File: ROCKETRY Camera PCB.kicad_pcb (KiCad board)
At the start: 2 copper layers, 111.8 x 75.7 mm, 38 parts, among them J1 Conn_01x03_Pin, J2 Conn_01x01_Pin, J3 Conn_01x01_Pin, J4 Conn_01x01_Pin, Q1 IRF7780M, U1 3.4v, U2 3.4v, U4 AP62200WU

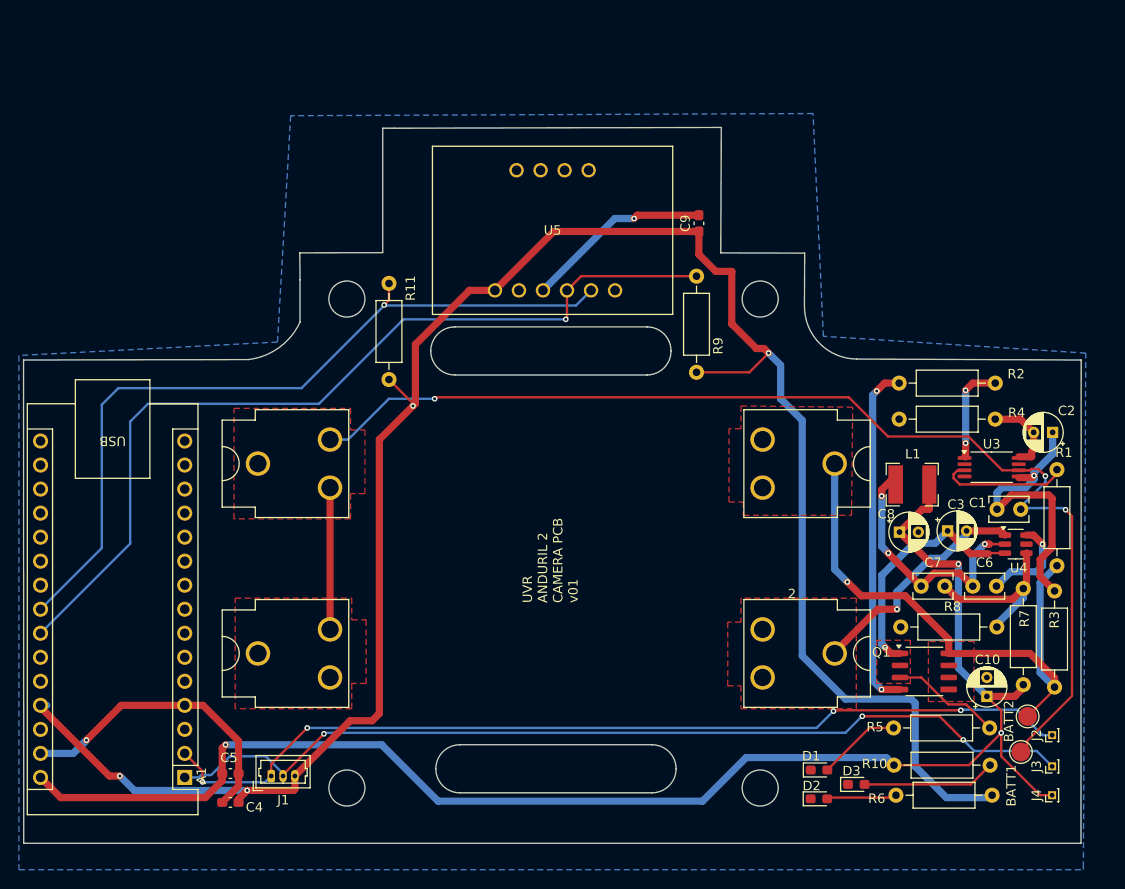
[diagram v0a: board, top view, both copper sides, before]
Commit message: swapped tht components with smt, in progress of routing traces. Board will be waaaaay cleaner
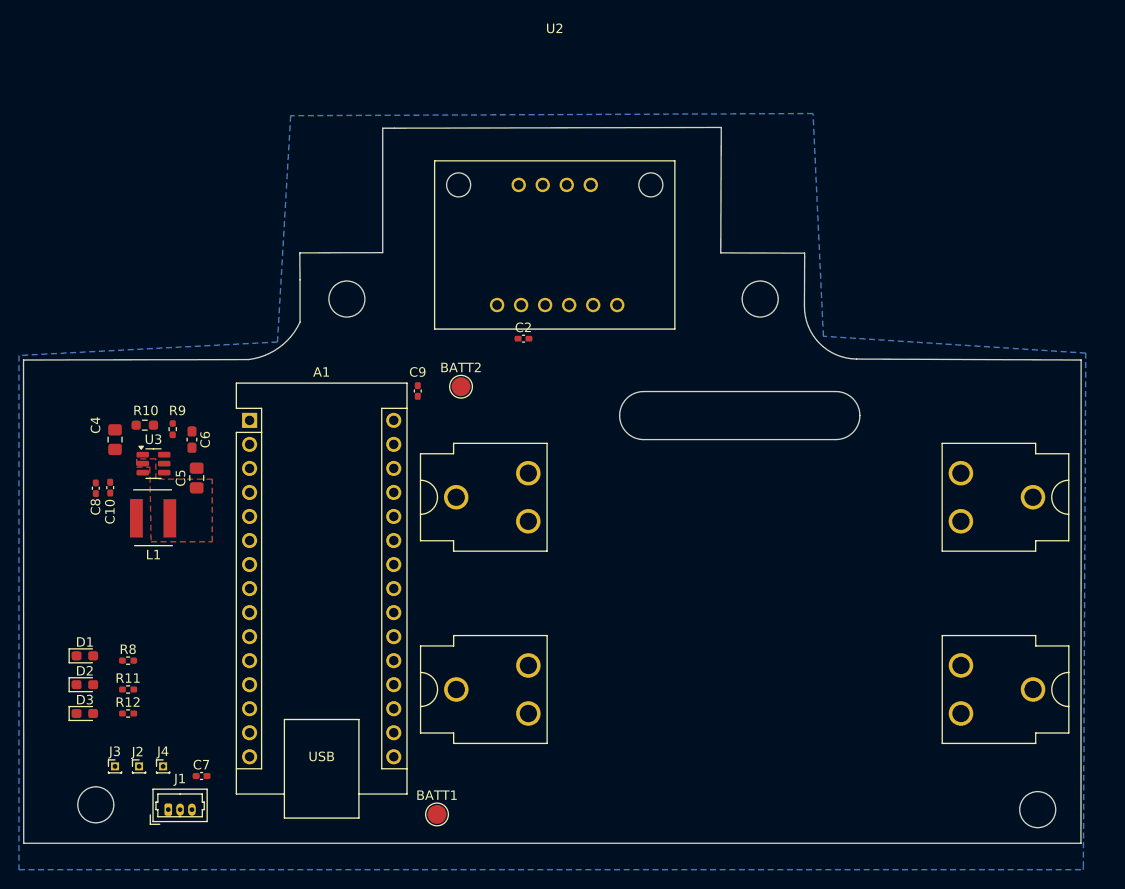
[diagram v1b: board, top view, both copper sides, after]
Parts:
- removed C1: 0.1uF, Capacitor_THT:C_Rect_L4.0mm_W2.5mm_P2.50mm
- removed C3: 10uF, Capacitor_THT:CP_Radial_D4.0mm_P2.00mm
- removed Q1: IRF7780M, Package_SO:SO-8_3.9x4.9mm_P1.27mm
- removed R1, R2: 5.1k, Resistor_THT:R_Axial_DIN0207_L6.3mm_D2.5mm_P10.16mm_Horizontal
- removed R3: 1k, Resistor_THT:R_Axial_DIN0207_L6.3mm_D2.5mm_P10.16mm_Horizontal
- removed R4: 51, Resistor_THT:R_Axial_DIN0207_L6.3mm_D2.5mm_P10.16mm_Horizontal
- removed R5, R6: 10k, Resistor_THT:R_Axial_DIN0207_L6.3mm_D2.5mm_P10.16mm_Horizontal
- removed R7: 52k, Resistor_THT:R_Axial_DIN0207_L6.3mm_D2.5mm_P10.16mm_Horizontal
- removed U1: 3.4v, CUSTOM_footprints:BatteryClip_Keystone_54_D16-19mm
- removed U4: AP62200WU, Package_TO_SOT_SMD:TSOT-23-6
- removed U5: ~, CUSTOM_footprints:ADX375L
- added BT1: 3.6V, CUSTOM_footprints:BatteryClip_Keystone_54_D16-19mm, F.Cu at (127.5, 89.4)
- added BT2: 3.6V, CUSTOM_footprints:BatteryClip_Keystone_54_D16-19mm, F.Cu at (127.5, 109.7)
- added R12: 1k, Resistor_SMD:R_0402_1005Metric_Pad0.72x0.64mm_HandSolder, F.Cu at (94.9, 112.3)
- C10, C8: footprint Capacitor_THT:CP_Radial_D4.0mm_P2.00mm -> Capacitor_SMD:C_0402_1005Metric_Pad0.74x0.62mm_HandSolder
- C2: value 2.2uF -> 100nF; footprint Capacitor_THT:CP_Radial_D4.0mm_P2.00mm -> Capacitor_SMD:C_0402_1005Metric_Pad0.74x0.62mm_HandSolder
- C4: value 100uF -> 10uF; footprint Capacitor_SMD:C_0603_1608Metric_Pad1.08x0.95mm_HandSolder -> Capacitor_SMD:C_0805_2012Metric_Pad1.18x1.45mm_HandSolder
- C5: value 100nF -> 330nF; footprint Capacitor_SMD:C_0603_1608Metric_Pad1.08x0.95mm_HandSolder -> Capacitor_SMD:C_0805_2012Metric_Pad1.18x1.45mm_HandSolder
- C6: value 200nF -> 100pF; footprint Capacitor_THT:C_Rect_L4.0mm_W2.5mm_P2.50mm -> Capacitor_SMD:C_0603_1608Metric_Pad1.08x0.95mm_HandSolder
- C7: value 20pF -> 100nF; footprint Capacitor_THT:C_Rect_L4.0mm_W2.5mm_P2.50mm -> Capacitor_SMD:C_0402_1005Metric_Pad0.74x0.62mm_HandSolder
- C9: footprint Capacitor_SMD:C_0603_1608Metric_Pad1.08x0.95mm_HandSolder -> Capacitor_SMD:C_0402_1005Metric_Pad0.74x0.62mm_HandSolder
- L1: footprint Inductor_SMD:L_Bourns-SRN5040 -> Inductor_SMD:BOURNS_SRN5040_CUSTOM
- R10: footprint Resistor_THT:R_Axial_DIN0207_L6.3mm_D2.5mm_P10.16mm_Horizontal -> Resistor_SMD:R_0603_1608Metric_Pad0.98x0.95mm_HandSolder
- R11, R8: value 10k -> 1k; footprint Resistor_THT:R_Axial_DIN0207_L6.3mm_D2.5mm_P10.16mm_Horizontal -> Resistor_SMD:R_0402_1005Metric_Pad0.72x0.64mm_HandSolder
- R9: value 10k -> 52.3k; footprint Resistor_THT:R_Axial_DIN0207_L6.3mm_D2.5mm_P10.16mm_Horizontal -> Resistor_SMD:R_0402_1005Metric_Pad0.72x0.64mm_HandSolder
- U2: value 3.4v -> ~; footprint CUSTOM_footprints:BatteryClip_Keystone_54_D16-19mm -> CUSTOM_footprints:ADX375L
- U3: value ~ -> AP62200WU; footprint Package_SO:TSSOP-8_4.4x3mm_P0.65mm -> Package_TO_SOT_SMD:TSOT-23-6
- moved J3 99.1 mm to (93.5, 117.9), turned to 0 degrees
- moved J2 96.6 mm to (96.0, 117.9), turned to 0 degrees
- moved C10 95.3 mm to (93.0, 88.4)
- moved J4 94.0 mm to (98.6, 117.9), turned to 0 degrees
- moved R8 91.9 mm to (94.9, 106.7), turned to 0 degrees
- moved U3 88.6 mm to (97.5, 85.9)
- moved R10 87.0 mm to (96.6, 81.8), turned to 180 degrees
- moved C8 85.1 mm to (91.4, 88.5), turned to 90 degrees
- moved C6 84.0 mm to (101.6, 83.3), turned to -90 degrees
- moved D3 81.9 mm to (90.3, 112.3)
- moved L1 80.9 mm to (97.5, 90.4)
- moved C7 78.7 mm to (102.6, 118.9)
- moved D1 78.5 mm to (90.3, 106.2)
- moved D2 78.5 mm to (90.3, 109.2)
- moved BATT2 69.3 mm to (130.0, 77.7)
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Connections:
- A1 pad 23: /A4 -> /SDA
- A1 pad 24: /A5 -> /SCL
- A1 pad 27: /+5V -> unconnected-(A1-+5V-Pad27)
- A1 pad 30: /5V -> +5V
- BATT1 pad 1: /V-mid -> +BATT
- BATT2 pad 1: /V-BATT+ -> VCC
- C10 pad 1: /5V -> +5V
- C2 pad 1: Net-(U3-VDD) -> +5V
- C2 pad 2: Net-(U3-VSS) -> GND
- C4 pad 1: /+5V -> VCC
- C4 pad 2: GND -> Net-(BT2--)
- C5 pad 1: GND -> Net-(U3-SW)
- C5 pad 2: /5V -> Net-(U3-BST)
- C6 pad 1: Net-(U4-SW) -> +5V
- C6 pad 2: Net-(U4-BST) -> Net-(U3-FB)
- C7 pad 1: Net-(U4-SW) -> +5V
- C7 pad 2: Net-(U4-FB) -> GND
- C8 pad 1: /5V -> +5V
- C9 pad 1: /+5V -> GND
- C9 pad 2: GND -> +5V
- J1 pad 3: /+5V -> +5V
- J4 pad 1: /5V -> +5V
- L1 pad 1: Net-(U4-SW) -> Net-(U3-SW)
- L1 pad 2: /5V -> +5V
- R10 pad 1: /5V -> Net-(U3-FB)
- R10 pad 2: Net-(D3-A) -> GND
- R11 pad 1: /+5V -> +5V
- R11 pad 2: /A4 -> Net-(D2-A)
- R8 pad 1: Net-(U4-FB) -> VCC
- R8 pad 2: GND -> Net-(D1-A)
- R9 pad 1: /+5V -> +5V
- R9 pad 2: /A5 -> Net-(U3-FB)
- U2 pad 1: /V-mid -> GND
- U2 pad 2: Net-(U2--) -> unconnected-(U2-I2-Pad2)
- U3 pad 1: /DOP -> VCC
- U3 pad 2: unconnected-(U3-COP-Pad2) -> Net-(U3-SW)
- U3 pad 3: /VMP -> Net-(BT2--)
- U3 pad 4: unconnected-(U3-CTL-Pad4) -> Net-(U3-BST)
- U3 pad 5: Net-(U3-VDD) -> unconnected-(U3-EN-Pad5)
- U3 pad 6: /V-mid -> Net-(U3-FB)
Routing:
- net /+5V: track 214.9 -> 0.00 mm, vias 4 -> 0
- net /5V: track 161.4 -> 0.00 mm, vias 3 -> 0
- net /V-mid: track 133.4 -> 0.00 mm, vias 3 -> 0
- net Net-(A1-D0/RX): track 98.9 -> 0.00 mm, vias 4 -> 0
- net Net-(A1-D1/TX): track 98.7 -> 0.00 mm, vias 3 -> 0
- net /A5: track 94.3 -> 0.00 mm, vias 1 -> 0
- net /A4: track 83.7 -> 0.00 mm, vias 1 -> 0
- net /V-BATT+: track 59.5 -> 0.00 mm, vias 1 -> 0
- net GND: track 53.2 -> 0.00 mm, vias 2 -> 0
- net /+7.4V: track 37.3 -> 0.00 mm, vias 1 -> 0
- net Net-(Q1-G): track 36.8 -> 0.00 mm, vias 2 -> 0
- net Net-(U3-VDD): track 31.0 -> 0.00 mm, vias 1 -> 0
- net Net-(U4-SW): track 27.7 -> 0.00 mm, vias 3 -> 0
- net Net-(U2--): track 24.9 -> 0.00 mm, vias 1 -> 0
- net Net-(U4-FB): track 18.9 -> 0.00 mm
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- added copper zone on F.Cu, net Net-(U3-SW)
- removed copper zone on F.Cu, net /+7.4V
- removed copper zone on F.Cu, net /V-BATT+
- removed copper zone on F.Cu, net /V-mid
- removed copper zone on F.Cu, net Net-(U2--)
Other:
- outline, holes or cut-outs redrawn
- board text removed: "2"
- board text removed: "UVR ANDURIL 2 CAMERA PCB v01"

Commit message: pcb ready for final review/ ordering
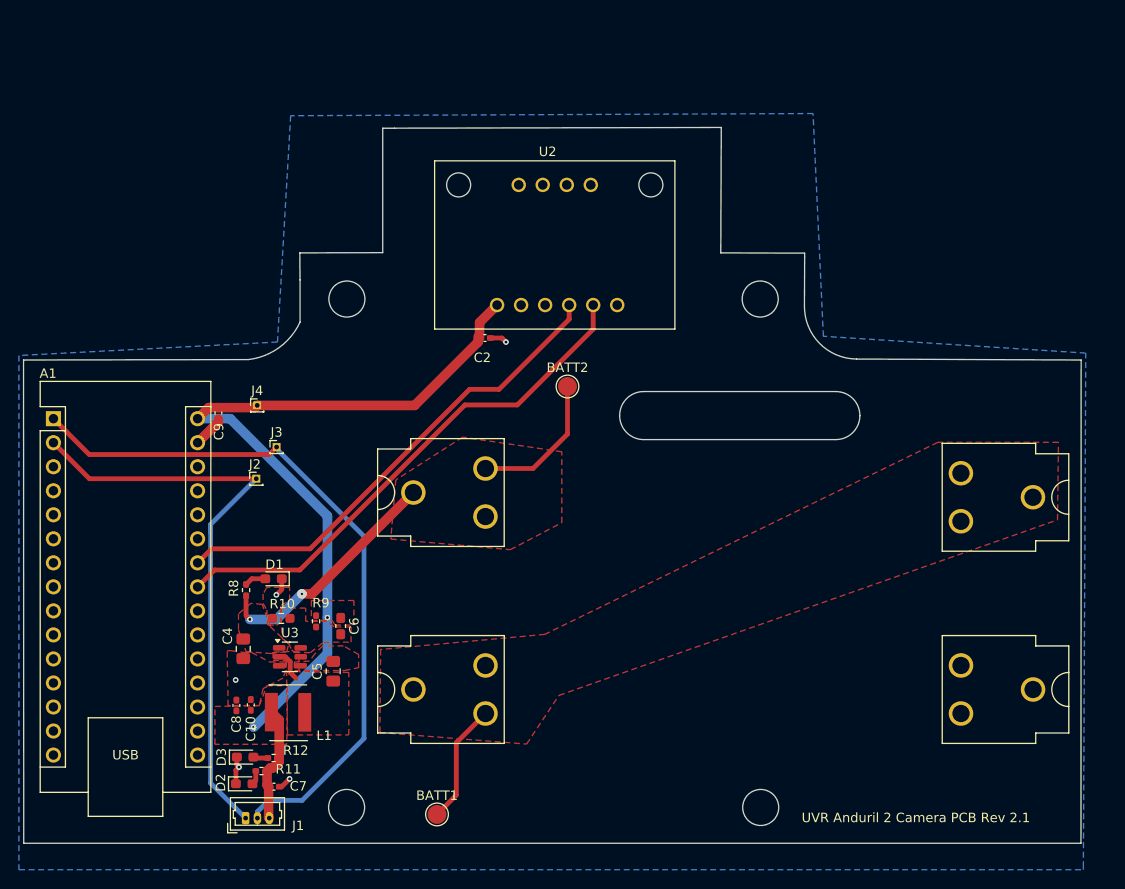
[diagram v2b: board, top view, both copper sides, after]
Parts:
- moved J4 39.4 mm to (108.5, 79.7)
- moved J3 37.8 mm to (110.5, 84.1)
- moved J2 32.8 mm to (108.4, 87.5)
- moved C10 27.4 mm to (107.8, 111.4)
- moved C8 27.4 mm to (106.3, 111.4)
- moved L1 27.0 mm to (111.7, 113.3), turned to 180 degrees
- moved C4 25.9 mm to (107.0, 105.4)
- moved R9 25.3 mm to (114.7, 102.5)
- moved C6 25.2 mm to (117.3, 103.0)
- moved C5 25.0 mm to (116.5, 107.8)
- moved R10 25.0 mm to (111.0, 102.2)
- moved U3 25.0 mm to (112.0, 106.3)
- moved D1 21.5 mm to (110.2, 98.0), turned to 180 degrees
- moved C9 21.2 mm to (104.4, 80.5), turned to 90 degrees
- moved A1 20.7 mm to (87.0, 81.1)
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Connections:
- BT2 pad 2: Net-(BT2--) -> GND
- C4 pad 2: Net-(BT2--) -> GND
- D1 pad 1: Net-(D1-K) -> GND
- D2 pad 1: Net-(D2-K) -> GND
- D3 pad 1: Net-(D3-K) -> GND
- U3 pad 3: Net-(BT2--) -> GND
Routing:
- net +5V: track 0.00 -> 93.7 mm, vias 0 -> 2
- net Net-(A1-D1/TX): track 0.00 -> 75.3 mm
- net Net-(A1-D0/RX): track 0.00 -> 63.0 mm
- net /SDA: track 0.00 -> 55.6 mm
- net /SCL: track 0.00 -> 51.4 mm
- net VCC: track 0.00 -> 40.6 mm, vias 0 -> 2
- net +BATT: track 0.00 -> 12.8 mm
- net GND: track 0.00 -> 11.7 mm, vias 0 -> 5
- net Net-(U3-SW): track 0.00 -> 3.40 mm
- net Net-(D1-A): track 0.00 -> 2.27 mm
- net Net-(D3-A): track 0.00 -> 1.57 mm
- net Net-(D2-A): track 0.00 -> 1.50 mm
- added copper zone on F.Cu, net +5V
- added copper zone on F.Cu, net +BATT
- added copper zone on F.Cu, net GND
- added copper zone on F.Cu, net Net-(U3-BST)
- added copper zone on F.Cu, net Net-(U3-FB)
- added copper zone on F.Cu, net VCC
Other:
- outline, holes or cut-outs redrawn
- rule pad_to_mask_clearance: 0 -> 0.038
- board text added: "UVR Anduril 2 Camera PCB Rev 2.1"

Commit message: adding curves to pcb edges
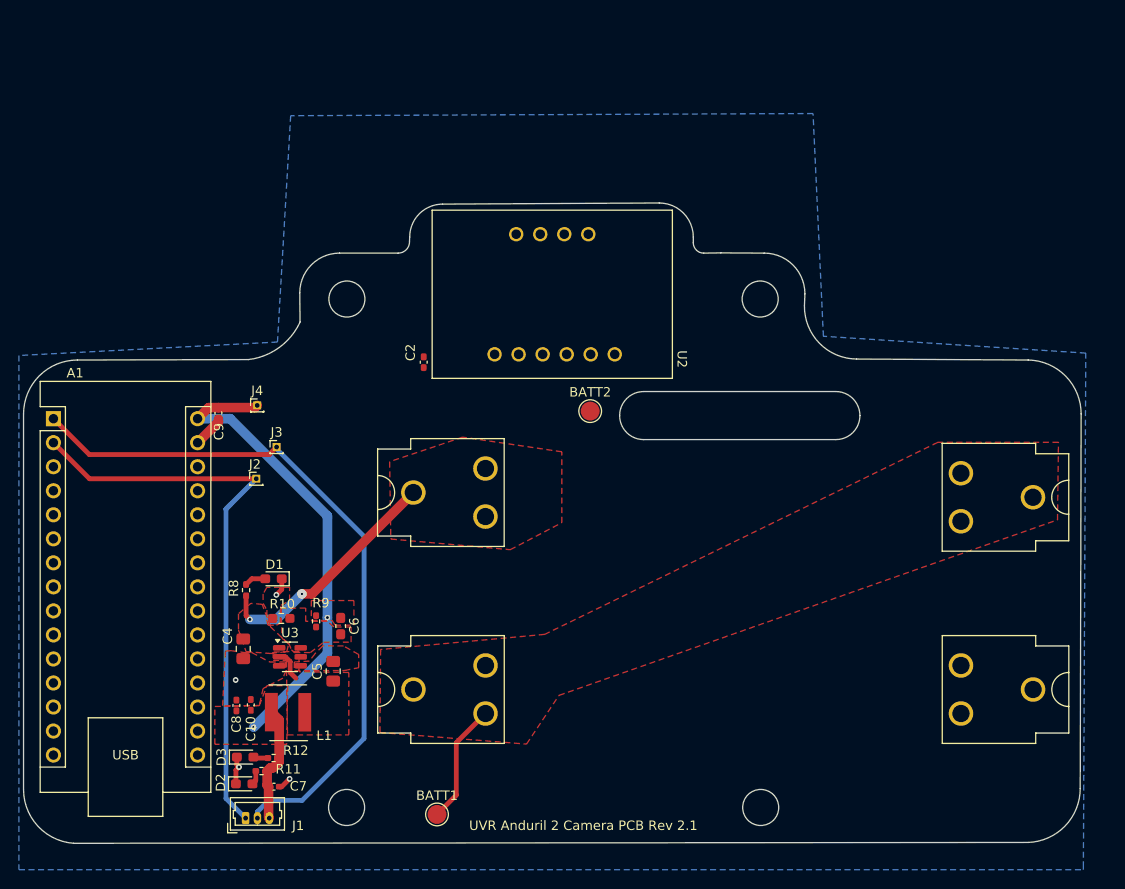
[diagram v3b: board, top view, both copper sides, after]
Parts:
- moved C2 6.96 mm to (126.1, 75.1), turned to 90 degrees
- moved U2 5.22 mm to (139.7, 68.0)
- moved BATT2 3.54 mm to (143.7, 80.3)
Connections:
- C4 pad 1: VCC -> Net-(J5-Pin_1)
- D2 pad 1: GND -> Net-(D2-K)
- R8 pad 1: VCC -> Net-(J5-Pin_1)
- U3 pad 1: VCC -> Net-(J5-Pin_1)
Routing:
- net /SDA: track 55.6 -> 0.00 mm
- net /SCL: track 51.4 -> 0.00 mm
- net +5V: track 93.7 -> 62.8 mm
- net VCC: track 40.6 -> 25.4 mm
- net GND: track 11.7 -> 9.89 mm, vias 5 -> 4
- net Net-(A1-D0/RX): track 63.0 -> 61.8 mm
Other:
- board size 111.8 x 75.7 mm -> 111.8 x 67.7 mm

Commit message: added curves to pcb edges, added connector for screw switch
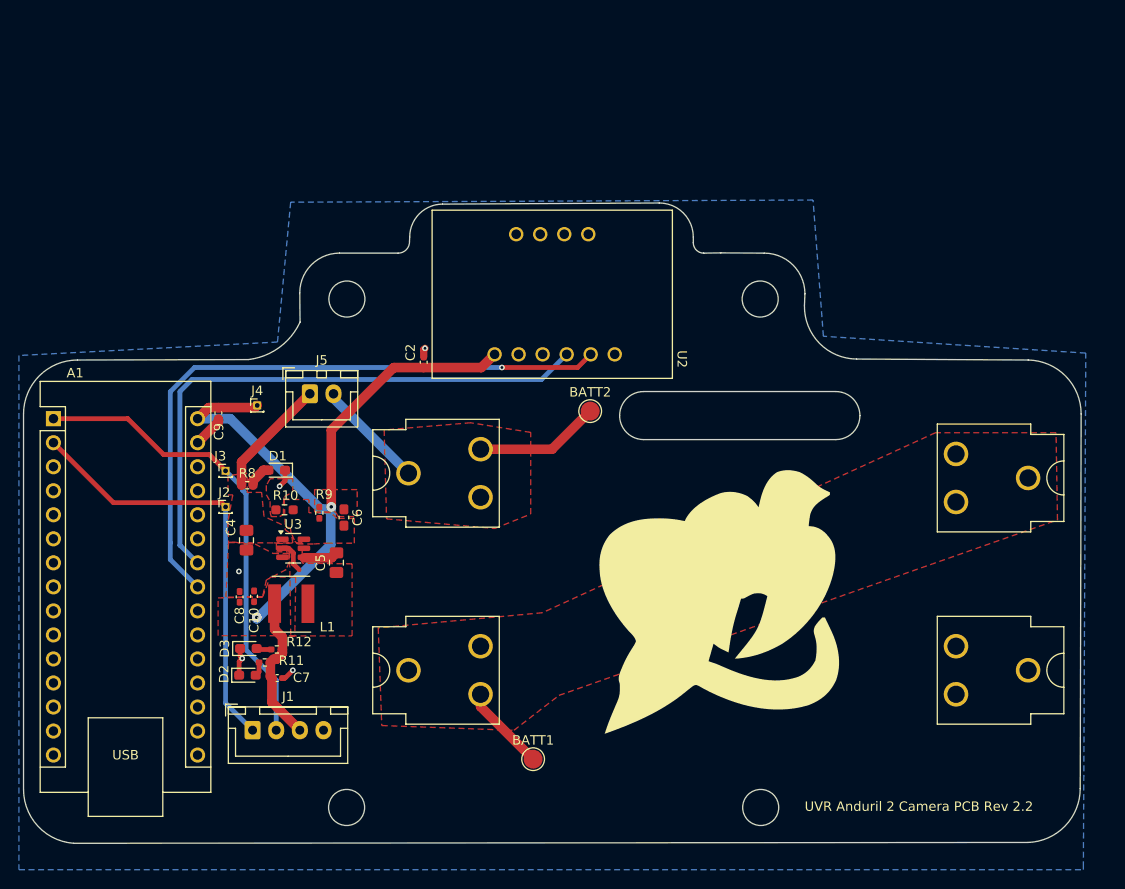
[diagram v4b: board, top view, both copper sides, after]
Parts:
- added J5: Conn_01x02_Pin, Connector_JST:JST_XH_B2B-XH-A_1x02_P2.50mm_Vertical, F.Cu at (114.1, 78.5)
- J1: footprint Connector_Molex:Molex_PicoBlade_53047-0310_1x03_P1.25mm_Vertical -> Connector_JST:JST_XH_B4B-XH-A_1x04_P2.50mm_Vertical
- moved BATT1 11.7 mm to (137.7, 117.1)
- moved C10 11.5 mm to (108.2, 99.9)
- moved C5 11.5 mm to (116.9, 96.3)
- moved C6 11.5 mm to (117.7, 91.5)
- moved C8 11.5 mm to (106.6, 99.9)
- moved D1 11.5 mm to (110.6, 86.5)
- moved D2 11.5 mm to (107.5, 108.2)
- moved D3 11.5 mm to (107.6, 105.4)
- moved L1 11.5 mm to (112.1, 101.9)
- moved R11 11.5 mm to (109.3, 106.9)
- moved R12 11.5 mm to (110.6, 105.5)
- moved R9 11.5 mm to (115.1, 91.0)
- moved U3 11.5 mm to (112.3, 94.8)
- moved C4 11.5 mm to (107.4, 93.9)
- moved C7 11.5 mm to (110.6, 108.5)
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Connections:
- D2 pad 1: Net-(D2-K) -> GND
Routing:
- net /SDA: track 0.00 -> 67.9 mm, vias 0 -> 1
- net /SCL: track 0.00 -> 61.4 mm
- net Net-(A1-D1/TX): track 75.3 -> 50.1 mm
- net +5V: track 62.8 -> 85.2 mm
- net Net-(A1-D0/RX): track 61.8 -> 45.8 mm
- net Net-(J5-Pin_1): track 0.00 -> 12.7 mm
- net Net-(U3-BST): track 0.00 -> 3.65 mm
- net +BATT: track 12.8 -> 9.16 mm
- net GND: track 9.89 -> 10.9 mm, vias 4 -> 5
- net VCC: track 25.4 -> 24.9 mm, vias 2 -> 0
- added copper zone on F.Cu, net Net-(J5-Pin_1)
- removed copper zone on F.Cu, net Net-(U3-BST)
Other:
- board text added: "UVR Anduril 2 Camera PCB Rev 2.2"
- board text removed: "UVR Anduril 2 Camera PCB Rev 2.1"
